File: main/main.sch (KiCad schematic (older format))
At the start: 23 parts

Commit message: finished general board schematic
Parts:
- added C6, C7: 1u, symbol Device:C
- added J3: Conn_01x10_Female, symbol Connector:Conn_01x10_Female
- added J4: USB_B, Connector_USB:USB_B_OST_USB-B1HSxx_Horizontal, symbol Connector:USB_B
- added U5: MCP2221A-I_SL, Package_SO:SOIC-14_3.9x8.7mm_P1.27mm, symbol MCP2221A-I_SL:MCP2221A-I_SL
- C1, C2, C3, C4, C5: renamed from C?; footprint (none) -> Capacitor_SMD:C_1206_3216Metric
- J2: renamed from J?; footprint (none) -> footprints:5033981892
- R1, R2, R3, R4, R5, R6, R7, R8, R9: renamed from R?; footprint (none) -> Resistor_SMD:R_1210_3225Metric
- U3, U4: renamed from U?; footprint Package_SO:SOIC-14_3.9x8.7mm_P1.27mm -> Package_SO:TSSOP-14_4.4x5mm_P0.65mm
- gave numbers to parts that had none: 6
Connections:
- net +3V3: no longer J1.2 (VCC)
- net +5V: now also C7.2, J3.9 (Pin_9), J4.1 (VBUS), U5.1 (VDD)
- net GND: now also C6.1, C7.1, J3.10 (Pin_10), J4.4 (GND), J4.5 (Shield), U5.14 (VSS)
- net RST: now also U5.4 (~RST)
- net URX: now reaches U1.16 (PD2)
- net URX: now also U5.5 (URX)
- net UTX: now reaches U1.17 (PD3)
- net UTX: now also U5.6 (UTX)
- net at U1.22 (PC0): now also J3.1 (Pin_1)
- net at U1.23 (PC1): now also J3.2 (Pin_2)
- net at U1.24 (PC2): now also J3.3 (Pin_3)
- net at U1.25 (PC3): now also J3.4 (Pin_4)
- net at U1.26 (PC4): now also J3.5 (Pin_5)
- net at U1.27 (PC5): now also J3.6 (Pin_6)
- net at U1.28 (PC6): now also J3.7 (Pin_7)
- net at U1.29 (PC7): now also J3.8 (Pin_8)
- new net: C6.2, U5.11 (VUSB)
- new net: J4.2 (D-), U5.12 (D-)
- new net: J4.3 (D+), U5.13 (D+)
- no-connect marks 4 -> 28
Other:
- note added: "gpio and i2c are not used.\n"
- note added: "programmer config does not matter.\nonly common ground."
- moved on the sheet: R6, R7, R8, R9

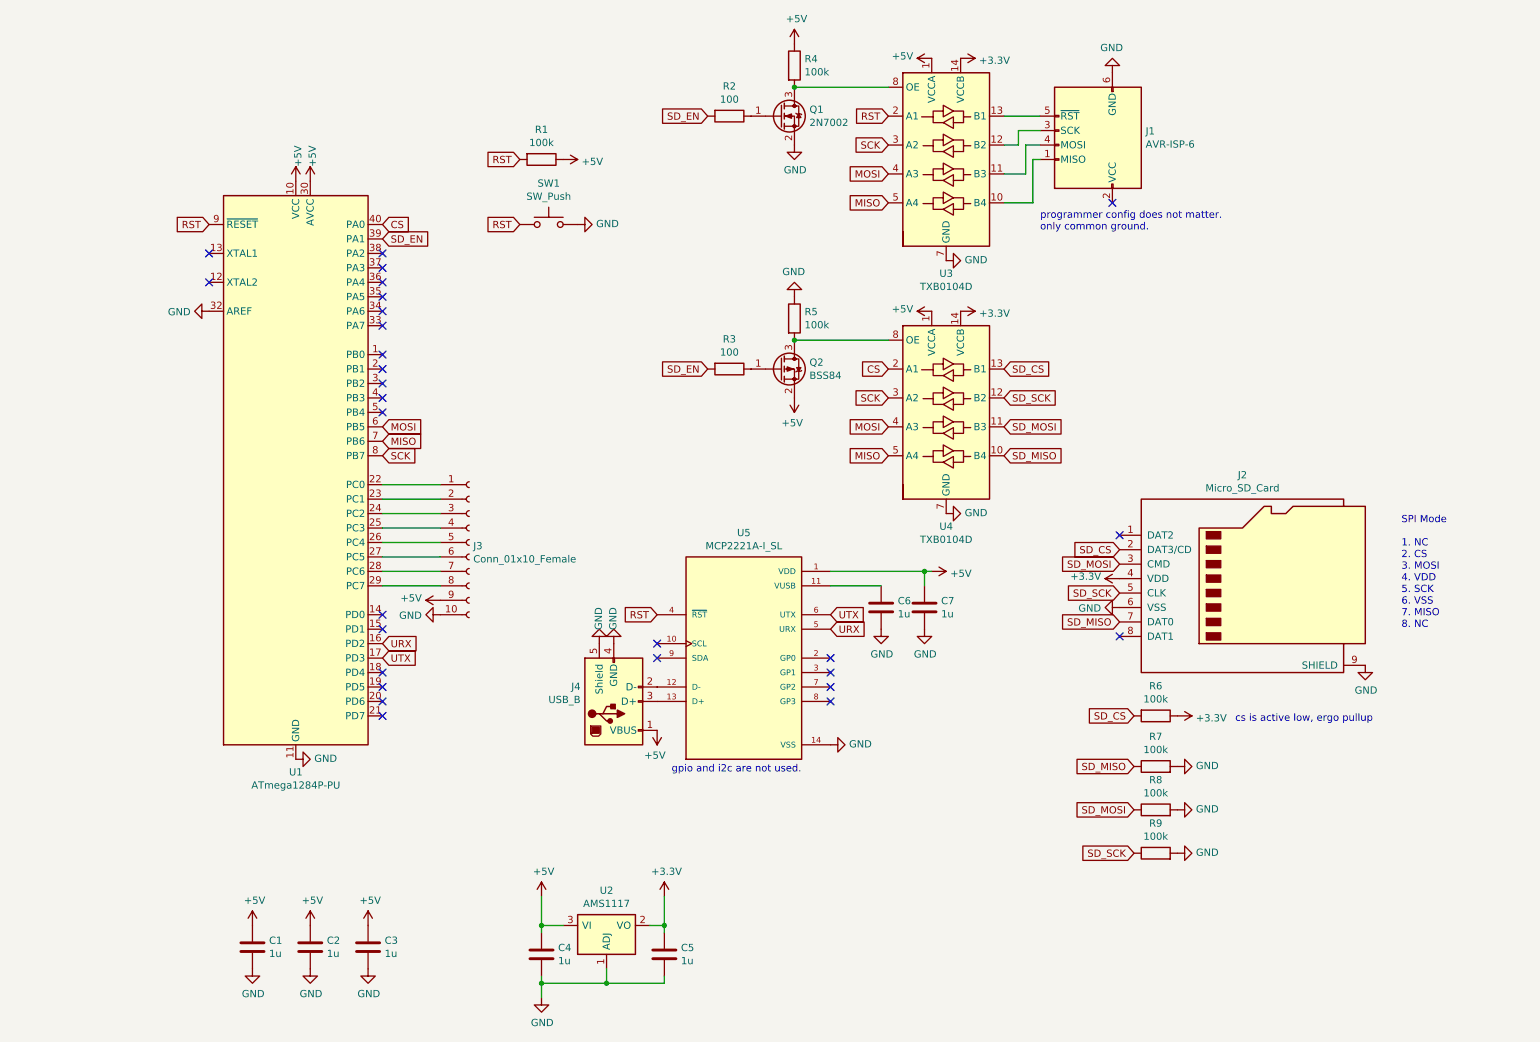
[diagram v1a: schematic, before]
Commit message: fixed footprints
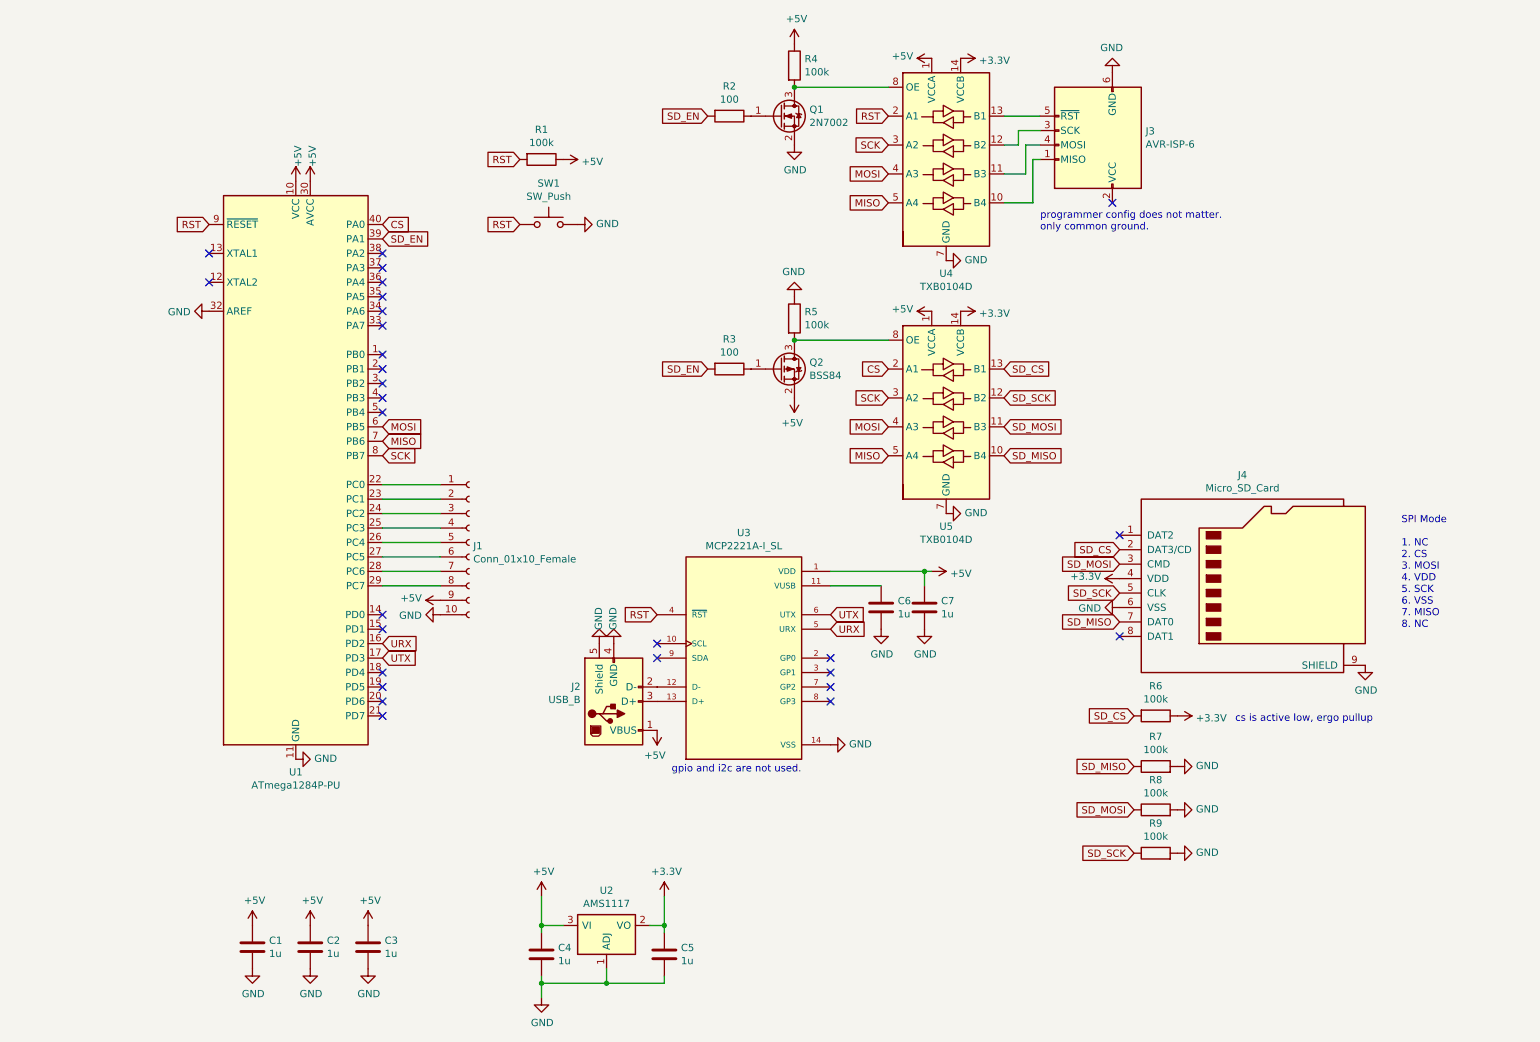
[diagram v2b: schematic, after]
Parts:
- C6, C7: footprint (none) -> Capacitor_SMD:C_1206_3216Metric
- J1: renamed from J3; footprint (none) -> Connector_PinSocket_2.54mm:PinSocket_1x10_P2.54mm_Vertical
- J3: renamed from J1; footprint (none) -> Connector_IDC:IDC-Header_2x03_P2.54mm_Vertical
- SW1: footprint (none) -> Button_Switch_SMD:SW_SPST_B3SL-1002P
- renumbered J4 to J2, J2 to J4, U5 to U3, U3 to U4, U4 to U5

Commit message: laid out pcb
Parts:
- added C8, C9: 1u, Capacitor_SMD:C_1206_3216Metric, symbol Device:C
- U1: footprint Package_DIP:DIP-40_W15.24mm -> Package_QFP:TQFP-44_10x10mm_P0.8mm
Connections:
- net +5V: now also C8.1, C9.1
- net GND: now also C8.2, C9.2
- net MISO: now also U4.4 (A3), U5.4 (A3); no longer U4.5 (A4), U5.5 (A4)
- net MOSI: now also U4.5 (A4), U5.5 (A4); no longer U4.4 (A3), U5.4 (A3)
- net SD_MISO: now also U5.11 (B3); no longer U5.10 (B4)
- net SD_MOSI: now also U5.10 (B4); no longer U5.11 (B3)
- net at U4.10 (B4): now also J3.4 (MOSI); no longer J3.1 (MISO)
- net at U4.11 (B3): now also J3.1 (MISO); no longer J3.4 (MOSI)
- net D-: now reaches J2.2 (D-), U3.12 (D-)
- net D+: now reaches J2.3 (D+), U3.13 (D+)
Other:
- moved on the sheet: J2
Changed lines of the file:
@@
 F 0 "U1" H 2900 1661 50  0000 C CNN
 F 1 "ATmega1284P-PU" H 2900 1570 50  0000 C CNN
-F 2 "Package_DIP:DIP-40_W15.24mm" H 2900 3750 50  0001 C CIN
+F 2 "Package_QFP:TQFP-44_10x10mm_P0.8mm" H 2900 3750 50  0001 C CIN
 F 3 "http://ww1.microchip.com/downloads/en/DeviceDoc/Atmel-8272-8-bit-AVR-microcontroller-ATmega164A_PA-324A_PA-644A_PA-1284_P_datasheet.pdf" H 2900 3750 50  0001 C CNN
 	1    2900 3750
@@
 Wire Wire Line
 	8050 1500 7950 1500
-Wire Wire Line
-	7950 1500 7950 1700
-Wire Wire Line
-	7950 1700 7800 1700
-Wire Wire Line
-	8050 1600 8000 1600
-Wire Wire Line
-	8000 1600 8000 1900
-Wire Wire Line
-	8000 1900 7800 1900
 $Comp
 L power:GND #PWR035
@@
 Text GLabel 7000 1500 0    50   Input ~ 0
 SCK
+Text GLabel 7000 1900 0    50   Input ~ 0
+MOSI
 Text GLabel 7000 1700 0    50   Input ~ 0
-MOSI
-Text GLabel 7000 1900 0    50   Input ~ 0
 MISO
 $Comp
@@
 Text GLabel 7800 3050 2    50   Input ~ 0
 SD_CS
-Text GLabel 7800 3450 2    50   Input ~ 0
+Text GLabel 7800 3650 2    50   Input ~ 0
 SD_MOSI
 Text GLabel 7800 3250 2    50   Input ~ 0
 SD_SCK
-Text GLabel 7800 3650 2    50   Input ~ 0
+Text GLabel 7800 3450 2    50   Input ~ 0
 SD_MISO
 Text GLabel 7000 3250 0    50   Input ~ 0
 SCK
+Text GLabel 7000 3650 0    50   Input ~ 0
+MOSI
 Text GLabel 7000 3450 0    50   Input ~ 0
-MOSI
-Text GLabel 7000 3650 0    50   Input ~ 0
 MISO
 Text GLabel 7000 3050 0    50   Input ~ 0
@@
 L Connector:USB_B J2
 U 1 1 692A58FC
-P 5100 5350
-F 0 "J2" H 4870 5247 50  0000 R CNN
-F 1 "USB_B" H 4870 5338 50  0000 R CNN
-F 2 "Connector_USB:USB_B_OST_USB-B1HSxx_Horizontal" H 5250 5300 50  0001 C CNN
-F 3 " ~" H 5250 5300 50  0001 C CNN
-	1    5100 5350
+P 4700 5350
+F 0 "J2" H 4470 5247 50  0000 R CNN
+F 1 "USB_B" H 4470 5338 50  0000 R CNN
+F 2 "Connector_USB:USB_B_OST_USB-B1HSxx_Horizontal" H 4850 5300 50  0001 C CNN
+F 3 " ~" H 4850 5300 50  0001 C CNN
+	1    4700 5350
 	1    0    0    1
 $EndComp
@@
 L power:GND #PWR017
 U 1 1 692B16A3
-P 5000 4950
-F 0 "#PWR017" H 5000 4700 50  0001 C CNN
-F 1 "GND" V 5005 4777 50  0000 C CNN
-F 2 "" H 5000 4950 50  0001 C CNN
-F 3 "" H 5000 4950 50  0001 C CNN
-	1    5000 4950
+P 4600 4950
+F 0 "#PWR017" H 4600 4700 50  0001 C CNN
+F 1 "GND" V 4605 4777 50  0000 C CNN
+F 2 "" H 4600 4950 50  0001 C CNN
+F 3 "" H 4600 4950 50  0001 C CNN
+	1    4600 4950
 	-1   0    0    1
 $EndComp
@@
 L power:GND #PWR018
 U 1 1 692B1EE7
-P 5100 4950
-F 0 "#PWR018" H 5100 4700 50  0001 C CNN
-F 1 "GND" V 5105 4777 50  0000 C CNN
-F 2 "" H 5100 4950 50  0001 C CNN
-F 3 "" H 5100 4950 50  0001 C CNN
-	1    5100 4950
+P 4700 4950
+F 0 "#PWR018" H 4700 4700 50  0001 C CNN
+F 1 "GND" V 4705 4777 50  0000 C CNN
+F 2 "" H 4700 4950 50  0001 C CNN
+F 3 "" H 4700 4950 50  0001 C CNN
+	1    4700 4950
 	-1   0    0    1
 $EndComp
@@
 Connection ~ 7250 4450
 Wire Wire Line
-	7250 4450 6600 4450
-Wire Wire Line
 	7250 4450 7250 4550
 $Comp
 L power:+5V #PWR019
 U 1 1 6930C984
-P 5400 5550
-F 0 "#PWR019" H 5400 5400 50  0001 C CNN
-F 1 "+5V" H 5415 5723 50  0000 C CNN
-F 2 "" H 5400 5550 50  0001 C CNN
-F 3 "" H 5400 5550 50  0001 C CNN
-	1    5400 5550
+P 5000 5550
+F 0 "#PWR019" H 5000 5400 50  0001 C CNN
+F 1 "+5V" H 5015 5723 50  0000 C CNN
+F 2 "" H 5000 5550 50  0001 C CNN
+F 3 "" H 5000 5550 50  0001 C CNN
+	1    5000 5550
 	-1   0    0    1
 $EndComp
+$Comp
+L power:+5V #PWR045
+U 1 1 692B4C2A
+P 2250 6900
+F 0 "#PWR045" H 2250 6750 50  0001 C CNN
+F 1 "+5V" H 2265 7073 50  0000 C CNN
+F 2 "" H 2250 6900 50  0001 C CNN
+F 3 "" H 2250 6900 50  0001 C CNN
+	1    2250 6900
+	1    0    0    -1
+$EndComp
+$Comp
+L power:GND #PWR046
+U 1 1 692B4C30
+P 2250 7200
+F 0 "#PWR046" H 2250 6950 50  0001 C CNN
+F 1 "GND" H 2255 7027 50  0000 C CNN
+F 2 "" H 2250 7200 50  0001 C CNN
+F 3 "" H 2250 7200 50  0001 C CNN
+	1    2250 7200
+	1    0    0    -1
+$EndComp
+$Comp
+L Device:C C9
+U 1 1 692B4C36
+P 2250 7050
+F 0 "C9" H 2365 7096 50  0000 L CNN
+F 1 "1u" H 2365 7005 50  0000 L CNN
+F 2 "Capacitor_SMD:C_1206_3216Metric" H 2288 6900 50  0001 C CNN
+F 3 "~" H 2250 7050 50  0001 C CNN
+	1    2250 7050
+	1    0    0    -1
+$EndComp
+$Comp
+L power:+5V #PWR043
+U 1 1 692B661A
+P 1900 6900
+F 0 "#PWR043" H 1900 6750 50  0001 C CNN
+F 1 "+5V" H 1915 7073 50  0000 C CNN
+F 2 "" H 1900 6900 50  0001 C CNN
+F 3 "" H 1900 6900 50  0001 C CNN
+	1    1900 6900
+	1    0    0    -1
+$EndComp
+$Comp
+L power:GND #PWR044
+U 1 1 692B6620
+P 1900 7200
+F 0 "#PWR044" H 1900 6950 50  0001 C CNN
+F 1 "GND" H 1905 7027 50  0000 C CNN
+F 2 "" H 1900 7200 50  0001 C CNN
+F 3 "" H 1900 7200 50  0001 C CNN
+	1    1900 7200
+	1    0    0    -1
+$EndComp
+$Comp
+L Device:C C8
+U 1 1 692B6626
+P 1900 7050
+F 0 "C8" H 2015 7096 50  0000 L CNN
+F 1 "1u" H 2015 7005 50  0000 L CNN
+F 2 "Capacitor_SMD:C_1206_3216Metric" H 1938 6900 50  0001 C CNN
+F 3 "~" H 1900 7050 50  0001 C CNN
+	1    1900 7050
+	1    0    0    -1
+$EndComp
+Wire Wire Line
+	7950 1500 7950 1900
+Wire Wire Line
+	7950 1900 7800 1900
+Wire Wire Line
+	8050 1600 8050 1700
+Wire Wire Line
+	7800 1700 8050 1700
+Wire Wire Line
+	5000 5250 5250 5250
+Wire Wire Line
+	5400 5350 5150 5350
+Wire Wire Line
+	6600 4450 7250 4450
+Text GLabel 5150 5500 3    50   Input ~ 0
+D+
+Text GLabel 5250 5500 3    50   Input ~ 0
+D-
+Wire Wire Line
+	5150 5500 5150 5350
+Connection ~ 5150 5350
+Wire Wire Line
+	5150 5350 5000 5350
+Wire Wire Line
+	5250 5500 5250 5250
+Connection ~ 5250 5250
+Wire Wire Line
+	5250 5250 5400 5250
 $EndSCHEMATC

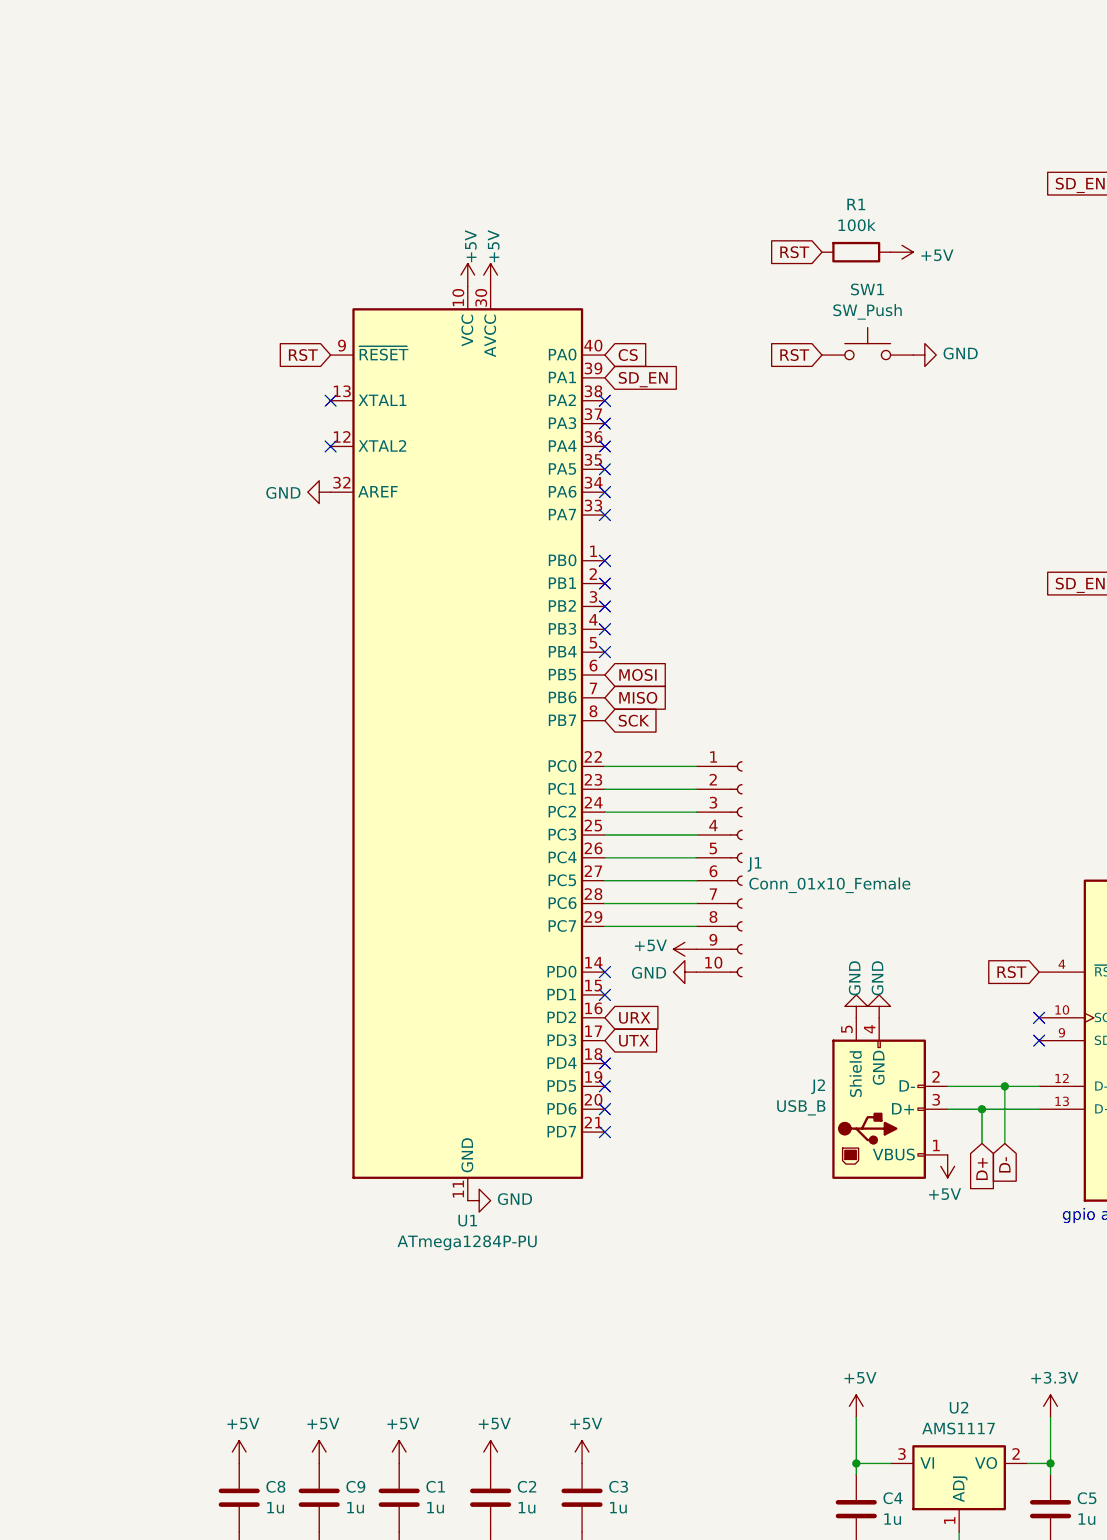
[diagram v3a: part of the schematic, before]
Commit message: added mounting holes
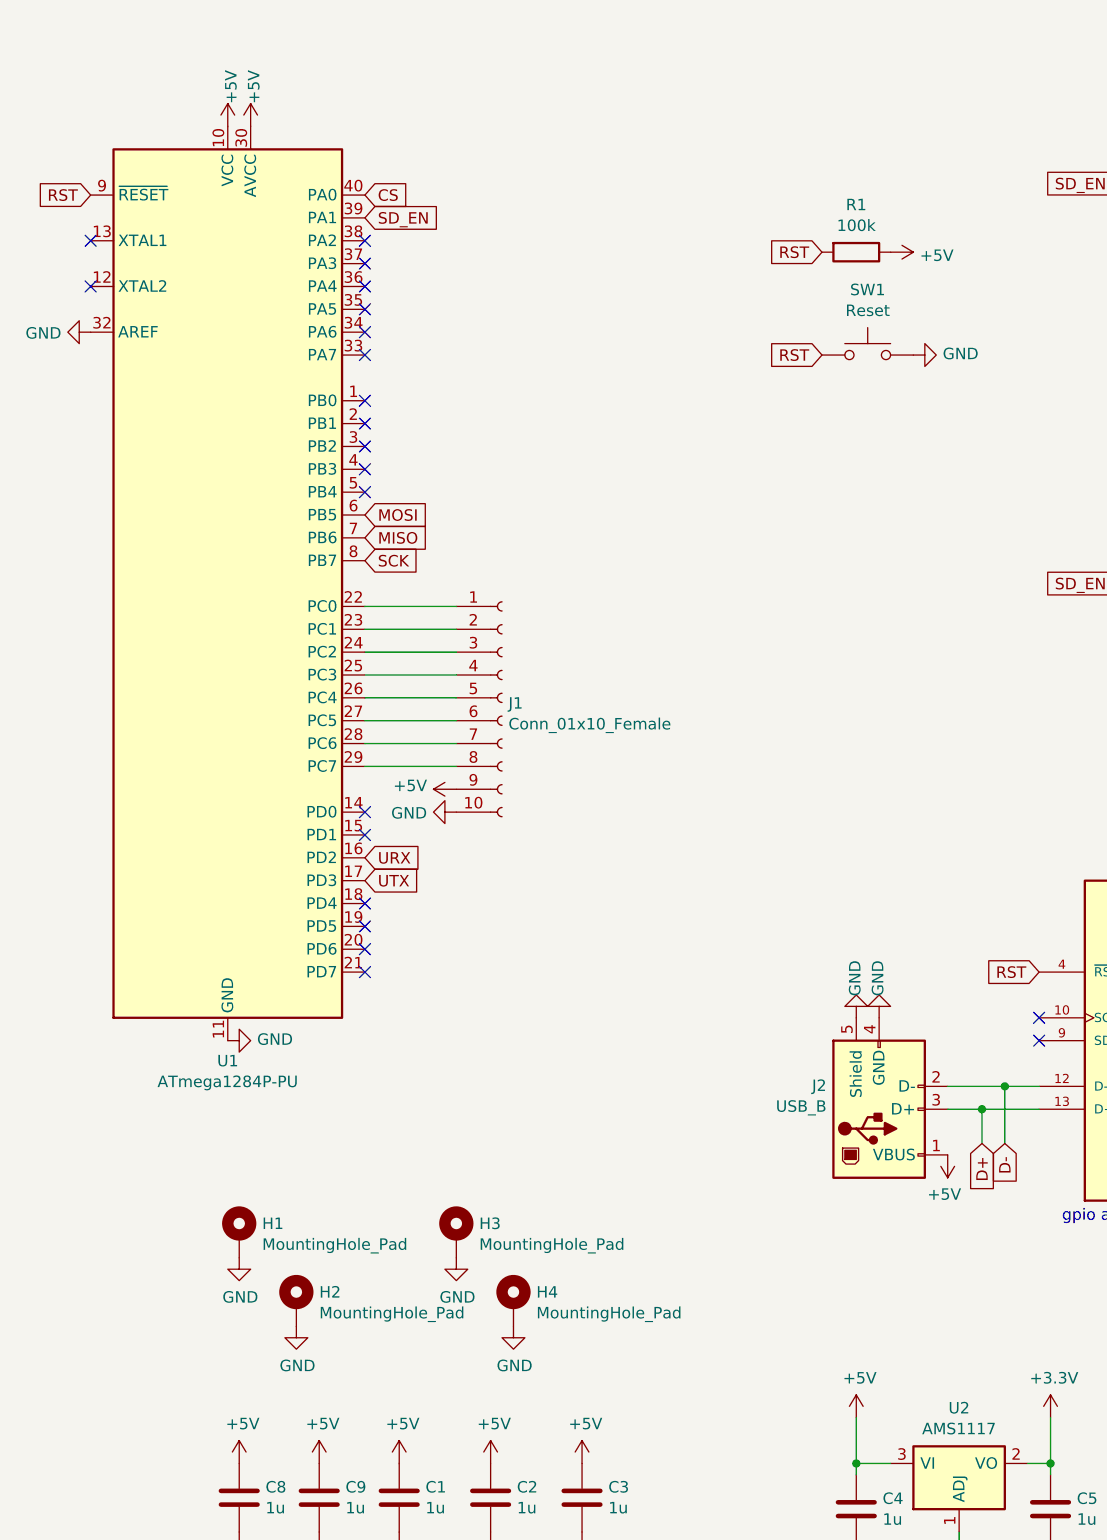
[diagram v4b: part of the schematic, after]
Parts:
- added H1, H2, H3, H4: MountingHole_Pad, MountingHole:MountingHole_3.2mm_M3_DIN965_Pad, symbol Mechanical:MountingHole_Pad
- SW1: value SW_Push -> Reset
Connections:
- net GND: now also H1.1, H2.1, H3.1, H4.1
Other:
- moved on the sheet: J1, U1
